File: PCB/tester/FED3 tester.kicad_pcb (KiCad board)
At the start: 4 copper layers, 108 x 134.4 mm, 166 parts, among them J1 USB4105-GF-A, J2 PR20203VBDN, J3 6pin_hd, J4 61300621021, J5 PPTC051LFBN-RC, J6 61300511021, J7 PPTC021LFBN-RC, K1 Relay SPDT, K2 Relay SPDT, K3 Relay SPDT, Q1 DMN63D8L-7, Q2 PMF170XP,115, Q3 DMN63D8L-7, Q4 DMN63D8L-7, Q5 DMN63D8L-7, Q6 DMN63D8L-7, SW1 TL3305BF260QG, SW2 TL3305BF260QG, SW3 TL3305BF260QG, SW4 TL3305BF260QG, SW5 TL3305BF260QG, SW6 TL3305BF260QG, SW7 TL3305BF260QG, SW8 TL3305BF260QG, SW9 TL3305BF260QG, U1 FT232RNL-REEL, U2 LP5907MFX-3.3, U3 LP5907MFX-3.3, U4 TPS73801DCQR, U5 ATXMEGA32A4U-MH, U6 THS4281, U7 THS4281, U8 THS4281, U9 ZXCT1082

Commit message: para revisão ao Filipe
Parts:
- removed the R37 at (145.8, 72.8)
- removed the R44 at (150.5, 67.5)
- removed the R45 at (158.4, 46.5)
- removed R47: 4.3k, Resistor_SMD:R_0603_1608Metric
- removed R49: 249k, Resistor_SMD:R_0402_1005Metric
- added C38: 100nF, Capacitor_SMD:C_0402_1005Metric, F.Cu at (147.5, 70.3)
- added R33: 1R, Resistor_SMD:R_0603_1608Metric, F.Cu at (142.0, 75.1)
- R35: renamed from R33; value 0.5R -> 1R; footprint Resistor_SMD:R_0805_2012Metric -> Resistor_SMD:R_0603_1608Metric
- R39: renamed from R36; value 5k -> 15R; footprint Resistor_SMD:R_0402_1005Metric -> Resistor_SMD:R_1206_3216Metric
- R7: value 8.2k -> 6.8k; footprint Resistor_SMD:R_0603_1608Metric -> Resistor_SMD:R_0402_1005Metric
- U9: value ZXCT1082 -> INA214AI; footprint Package_TO_SOT_SMD:SOT-23-5 -> Package_TO_SOT_SMD:SOT-363_SC-70-6
- moved R43 30.5 mm to (118.4, 82.2), turned to -90 degrees
- moved K2 16.6 mm to (153.4, 69.0), turned to -90 degrees
- moved D10 10.6 mm to (153.4, 61.0), turned to 0 degrees
- moved R34 9.90 mm to (154.0, 53.1), turned to -90 degrees
- moved R37 9.78 mm to (152.0, 53.1), turned to 90 degrees
- moved R39 9.42 mm to (142.8, 79.2), turned to 0 degrees
- moved R35 5.56 mm to (142.0, 77.0), turned to 180 degrees
- moved Q4 4.46 mm to (153.1, 56.9), turned to -90 degrees
- moved U9 3.39 mm to (146.2, 72.2), turned to 180 degrees
- renumbered D11 to D10, D9 to D11, D10 to D9, K2 to K1, K3 to K2, K1 to K3, Q6 to Q4, Q4 to Q6, R46 to R34, R34 to R36, R48 to R37, R43 to R42, R35 to R43, R39 to R44, R42 to R45
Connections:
- J3 pad 6: +3V3 -> unconnected-(J3-Pin_6-Pad6)
- J4 pad 1: +3V3 -> unconnected-(J4-Pin_1-Pad1)
- K2 pad 3: /main core/ADC Bat_I -> Net-(U9-IN+)
- K2 pad 5: Net-(K3-Pad5) -> Net-(K2-Pad5)
- K2 pad 7: unconnected-(K3-Pad7) (its old number) -> Net-(K2-Pad7)
- K3 pad 3: Net-(K1-Pad3) -> Net-(U9-IN+)
- R35 pad 1: Net-(K1-Pad3) -> Net-(K2-Pad7)
- R39 pad 1: Net-(U9-S+) -> /main core/DUT stage/VBatt_DUT
- R39 pad 2: Net-(K1-Pad3) -> Net-(K2-Pad5)
- R43 pad 2: Net-(K1-Pad3) -> Net-(U9-IN+)
- U9 pad 1: /main core/ADC Bat_I -> GND
- U9 pad 3: Net-(U9-S+) -> +3V3
- U9 pad 4: Net-(U9-S-) -> Net-(U9-IN+)
- U9 pad 5: USB+5V -> /main core/DUT stage/VBatt_DUT
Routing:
- net USB+5V: track 264.5 -> 189.9 mm, vias 7 -> 4
- net +3V3: track 597.4 -> 535.2 mm, vias 22 -> 21
- net Net-(U9-IN+): track 0.00 -> 46.0 mm, vias 0 -> 3
- net Net-(K1-Pad3): track 38.9 -> 0.00 mm, vias 3 -> 0
- net Net-(K2-Pad7): track 0.00 -> 19.0 mm
- net /main core/ADC Bat_I: track 72.5 -> 55.9 mm, vias 2 -> 3
- net Net-(K2-Pad5): track 0.00 -> 14.9 mm
- net /main core/DUT stage/VBatt_DUT: track 11.7 -> 19.2 mm
- net Net-(D10-A): track 17.2 -> 9.68 mm
- net /main core/RGBW_NOK: track 90.9 -> 95.3 mm
- net RELAY+5V: track 141.3 -> 138.1 mm
- net Net-(K3-Pad5): track 2.97 -> 0.00 mm
- net Net-(U9-S+): track 2.47 -> 0.00 mm
- net Net-(U9-S-): track 2.30 -> 0.00 mm
- net /main core/I_ON/OFF_Test: track 43.5 -> 41.5 mm, vias 3 -> 2
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
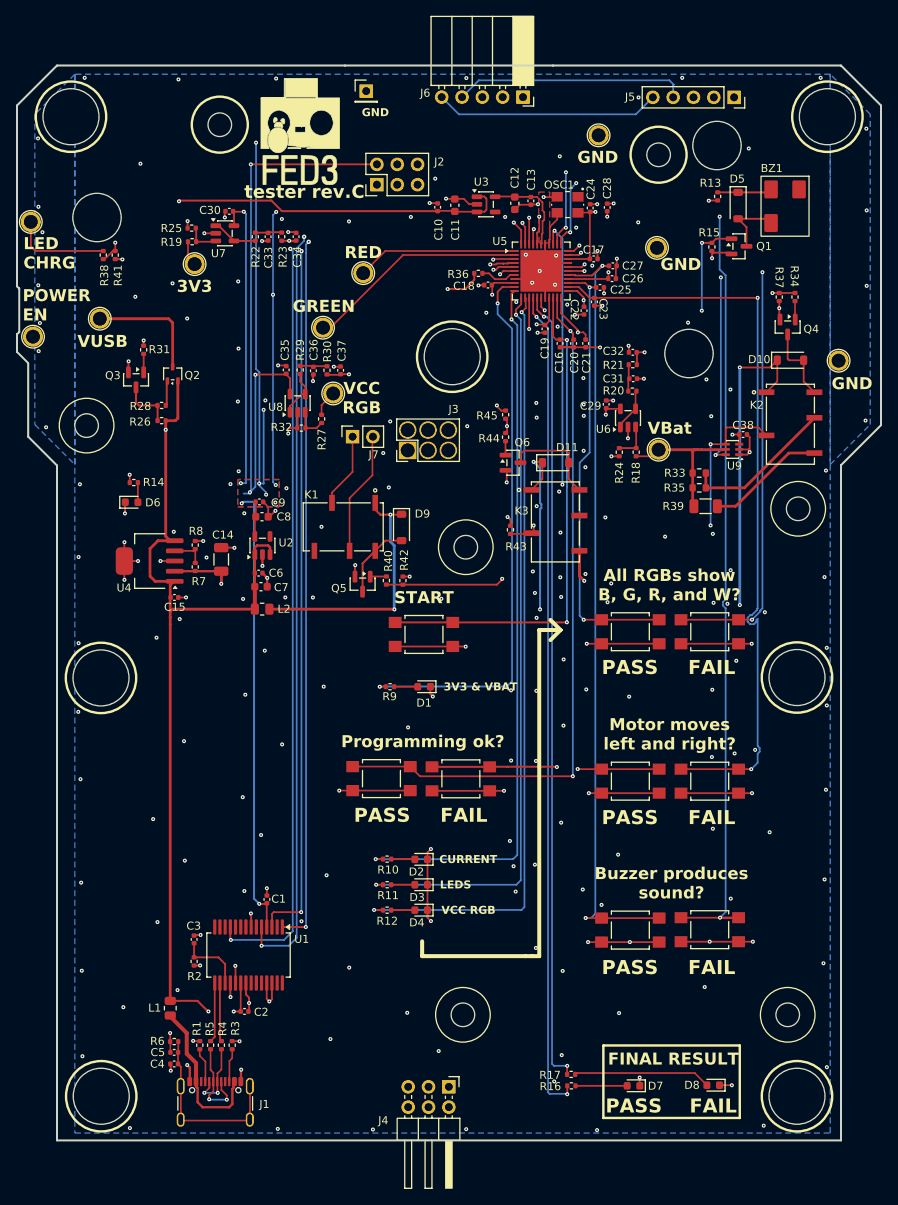
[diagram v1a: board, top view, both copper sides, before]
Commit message: 'limpeza' de Fab layer; tunnigs em poucas tracks
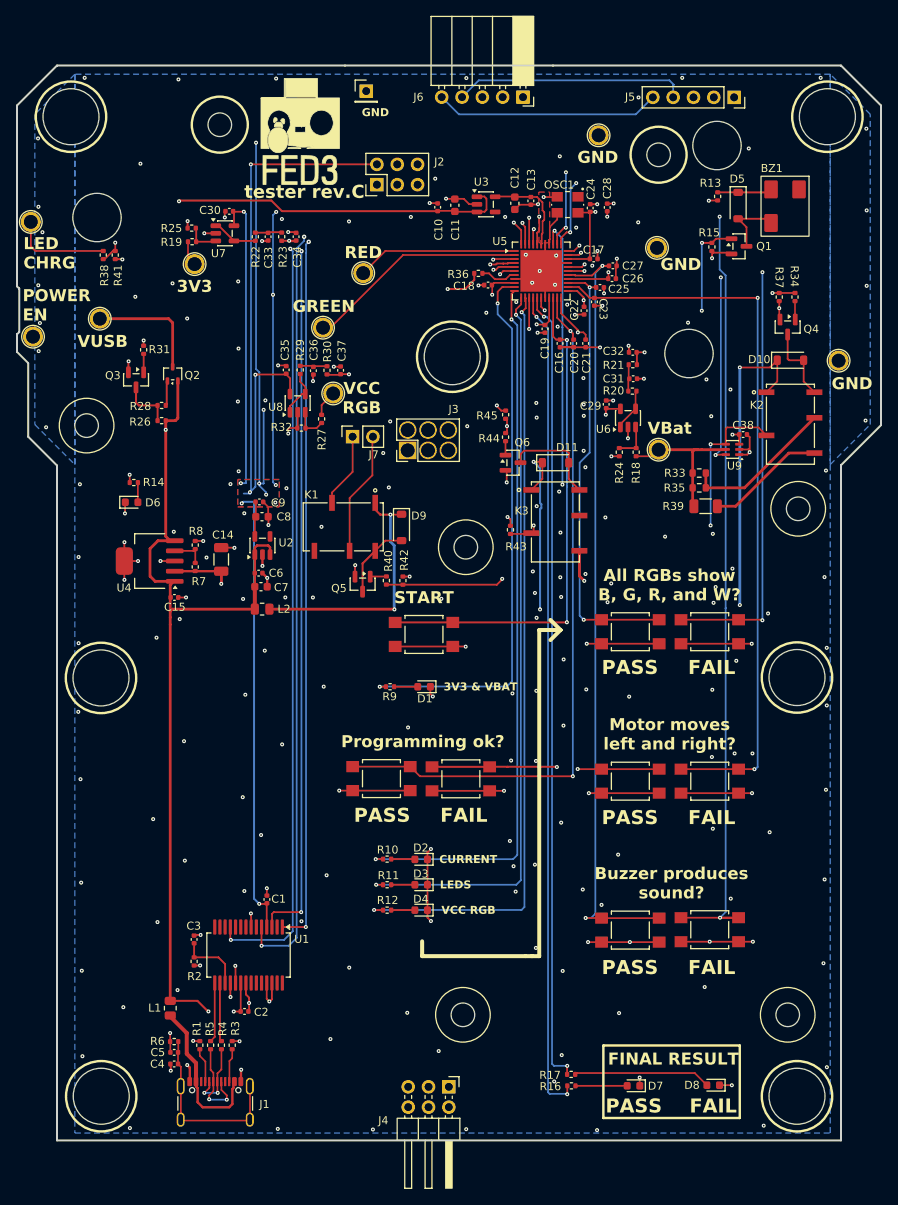
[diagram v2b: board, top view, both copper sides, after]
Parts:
- K1: value Relay SPDT -> K1
- K2: value Relay SPDT -> K2
- K3: value Relay SPDT -> K3
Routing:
- net /main core/RGBW_NOK: track 95.3 -> 92.6 mm
- net /main core/Motor_NOK: track 78.0 -> 78.8 mm
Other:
- board text added: "C29"
- board text added: "J3"

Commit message: fine tunning em fab Layer; pequenas modificações em routing
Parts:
- K1: value K1 -> Relay SPDT
- K2: value K2 -> Relay SPDT
- K3: value K3 -> Relay SPDT
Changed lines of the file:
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@@
 			)
 		)
-		(property "Value" "K3"
+		(property "Value" "Relay SPDT"
 			(at -0.61 -0.03 0)
 			(unlocked yes)
@@
 			)
 		)
-		(property "Value" "K2"
+		(property "Value" "Relay SPDT"
 			(at 0 0.2675 0)
 			(unlocked yes)
@@
 			)
 		)
-		(property "Value" "K1"
+		(property "Value" "Relay SPDT"
 			(at 0 0.2675 0)
 			(unlocked yes)
@@
 		(tags "capacitor")
 		(property "Reference" "C22"
-			(at -0.1 1.2 90)
+			(at 0.25 1.15 90)
 			(unlocked yes)
 			(layer "F.SilkS")
@@
 	)
 	(segment
+		(start 126.46 57.11804)
+		(end 126.13196 56.79)
+		(width 0.22)
+		(layer "F.Cu")
+		(net "/main core/Prog_NOK")
+	)
+	(segment
 		(start 126.826101 57.513051)
-		(end 126.8 57.48695)
+		(end 126.46 57.14695)
+		(width 0.22)
+		(layer "F.Cu")
+		(net "/main core/Prog_NOK")
+	)
+	(segment
+		(start 126.10305 56.79)
+		(end 124.74 55.42695)
 		(width 0.22)
 		(layer "F.Cu")
@@
 	)
 	(segment
-		(start 126.8 57.2)
-		(end 124.74 55.14)
+		(start 126.46 57.14695)
+		(end 126.46 57.11804)
+		(width 0.22)
+		(layer "F.Cu")
+		(net "/main core/Prog_NOK")
+	)
+	(segment
+		(start 124.74 55.42695)
+		(end 124.74 53.1786)
 		(width 0.22)
 		(layer "F.Cu")
@@
 	)
 	(segment
-		(start 126.8 57.48695)
-		(end 126.8 57.2)
+		(start 126.13196 56.79)
+		(end 126.10305 56.79)
 		(width 0.22)
 		(layer "F.Cu")
@@
 		(layer "F.Cu")
 		(net "/main core/Prog_NOK")
-	)
-	(segment
-		(start 124.74 55.14)
-		(end 124.74 53.1786)
-		(width 0.22)
-		(layer "F.Cu")
-		(net "/main core/Prog_NOK")
